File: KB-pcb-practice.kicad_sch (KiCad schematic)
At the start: 61 parts, among them J1 Conn_01x03, SW1 Reset, SW2 Boot, U1 RP2040, U2 IS31FL3742A-QFLS4-TR, U3 W25Q128JVS, U4 IS31FL3742A-QFLS4-TR, U5 NCP1117-3.3_SOT223, Y1 ABLS-12.000MHZ-B4-T

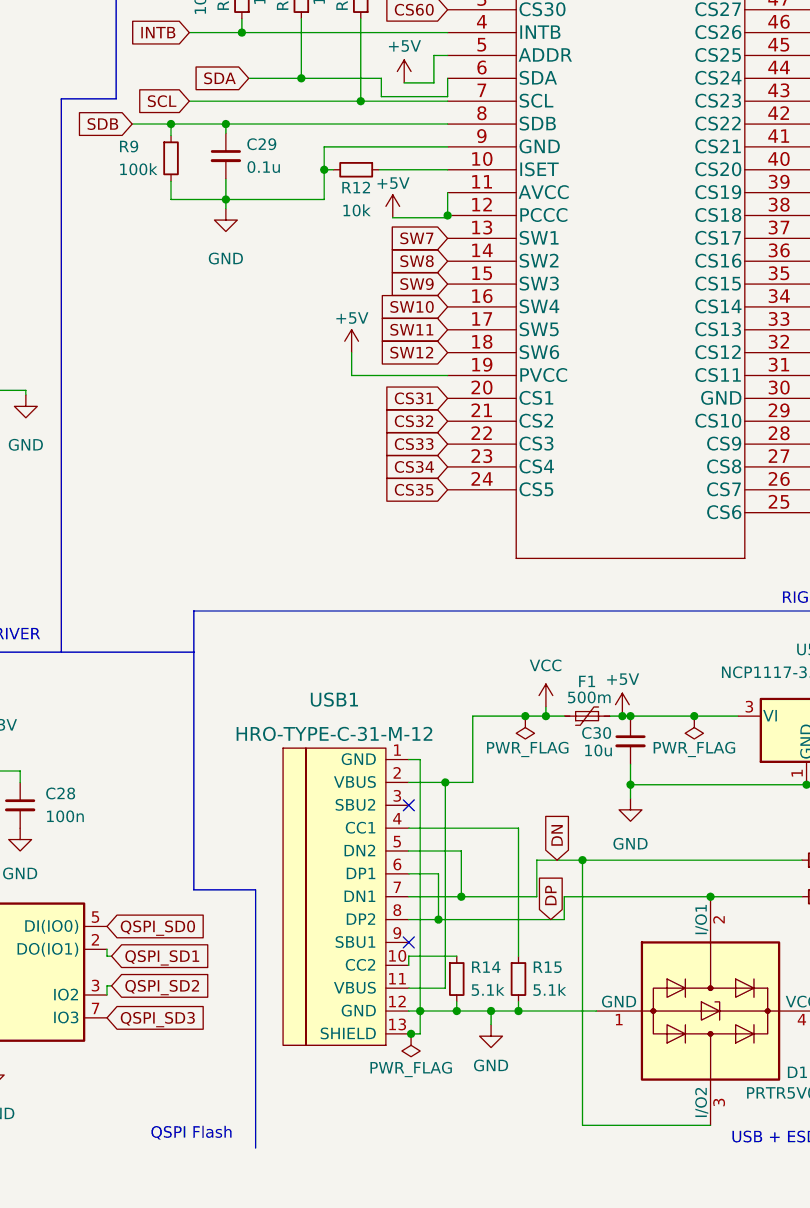
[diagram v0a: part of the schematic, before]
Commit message: Updated Schematic to match previous
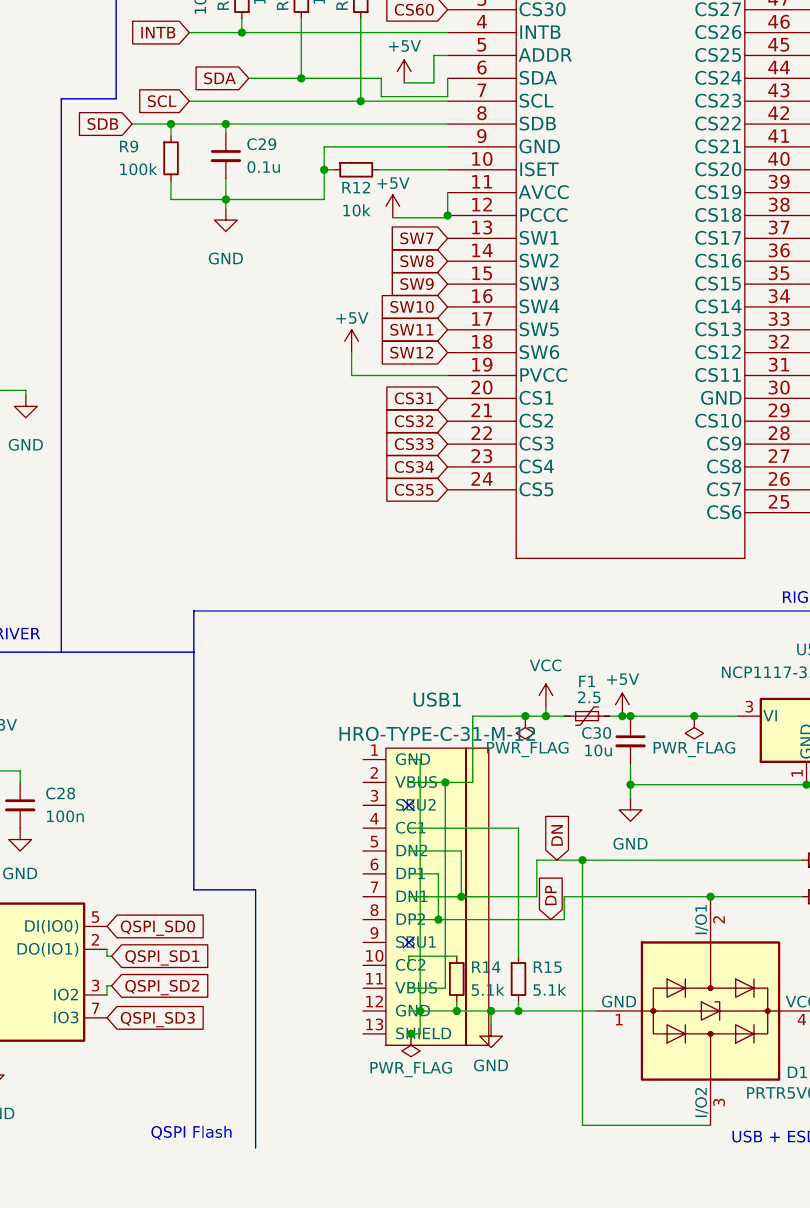
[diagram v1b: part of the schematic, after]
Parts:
- F1: value 500m -> 2.5
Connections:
- net DN: no longer USB1.5 (DN2), USB1.7 (DN1)
- net DP: no longer USB1.6 (DP1), USB1.8 (DP2)
- net GND: now also R12.1; no longer R12.2, USB1.1 (GND), USB1.12 (GND), USB1.13 (SHIELD)
- net VCC: no longer USB1.11 (VBUS), USB1.2 (VBUS)
- net at USB1.10 (CC2): no longer R14.1
- net at USB1.4 (CC1): no longer R15.1
- net at U4.10 (ISET): now also R12.2; no longer R12.1
- net  COL0 renamed COL0
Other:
- moved on the sheet: R12, USB1
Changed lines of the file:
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@@
     )
   )
-  (global_label " COL0" (shape input) (at 76.708 41.148 0) (fields_autoplaced)
+  (global_label "COL0" (shape input) (at 76.708 41.148 0) (fields_autoplaced)
     (effects (font (size 1.27 1.27)) (justify left))
-    (property "Intersheetrefs" "${INTERSHEET_REFS}" (at 85.4195 41.148 0)
+    (property "Intersheetrefs" "${INTERSHEET_REFS}" (at 84.4519 41.148 0)
       (effects (font (size 1.27 1.27)) (justify left) hide)
     )
@@
     )
   )
-  (symbol (lib_id "Type-C:HRO-TYPE-C-31-M-12") (at 222.504 136.906 0) (unit 1)
-    (in_bom yes) (on_board yes) (dnp no) (fields_autoplaced)
-    (property "Reference" "USB1" (at 216.789 116.332 0)
+  (symbol (lib_id "Type-C:HRO-TYPE-C-31-M-12") (at 222.504 136.906 0) (mirror y) (unit 1)
+    (in_bom yes) (on_board yes) (dnp no)
+    (property "Reference" "USB1" (at 228.219 116.332 0)
       (effects (font (size 1.524 1.524)))
     )
-    (property "Value" "HRO-TYPE-C-31-M-12" (at 216.789 120.142 0)
+    (property "Value" "HRO-TYPE-C-31-M-12" (at 228.219 120.142 0)
       (effects (font (size 1.524 1.524)))
     )
@@
     )
   )
-  (symbol (lib_id "Device:R_Small") (at 219.202 57.404 270) (unit 1)
+  (symbol (lib_id "Device:R_Small") (at 219.202 57.404 90) (mirror x) (unit 1)
     (in_bom yes) (on_board yes) (dnp no)
     (property "Reference" "R12" (at 219.202 59.436 90)
@@
       (effects (font (size 1.27 1.27)))
     )
-    (property "Value" "500m" (at 245.11 116.078 90)
-      (effects (font (size 1.27 1.27)))
-    )
+    (property "Value" "2.5" (at 245.11 116.078 90)
+      (effects (font (size 1.27 1.27)))
+    )

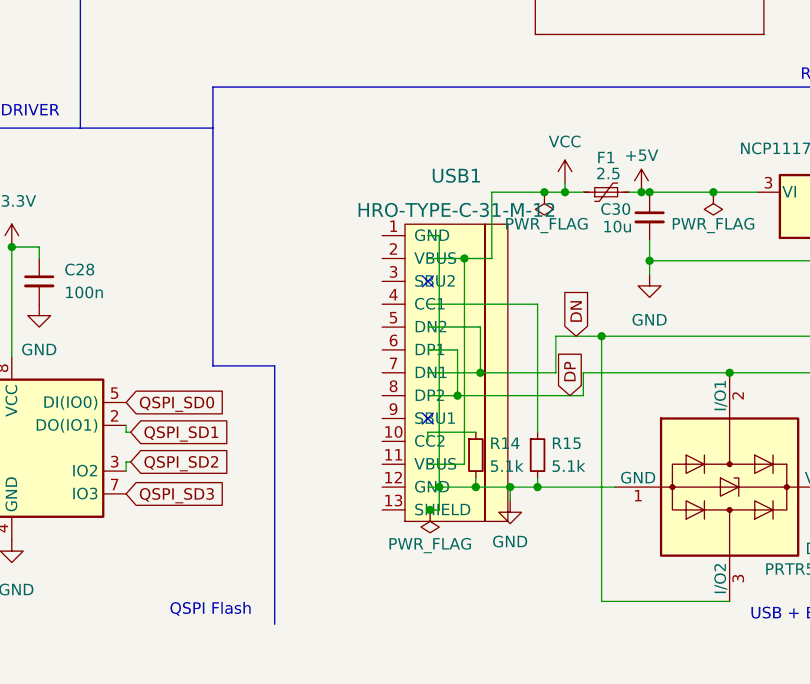
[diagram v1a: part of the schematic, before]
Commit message: Began Routing Columns and Rows
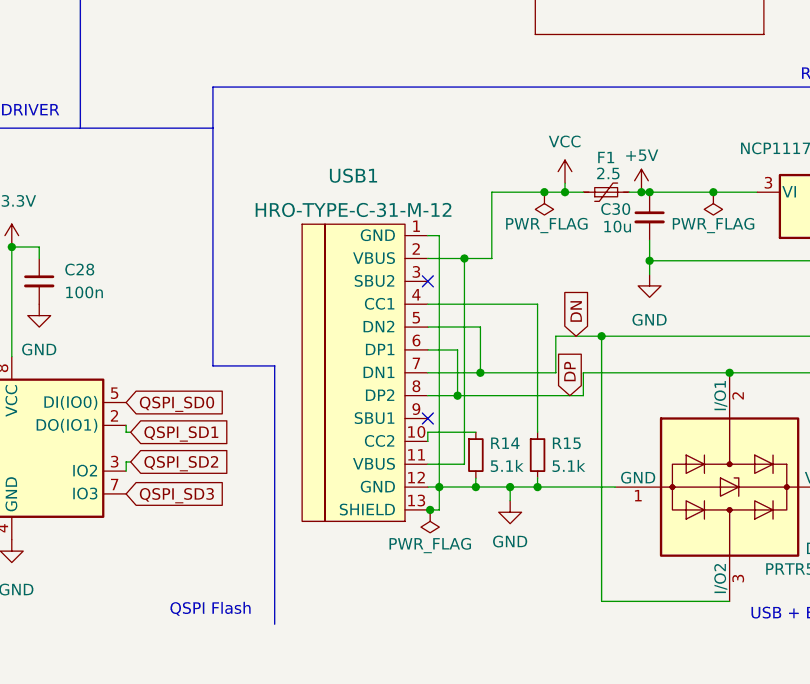
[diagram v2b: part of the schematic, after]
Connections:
- net DN: now also USB1.5 (DN2), USB1.7 (DN1)
- net DP: now also USB1.6 (DP1), USB1.8 (DP2)
- net GND: now also USB1.1 (GND), USB1.12 (GND), USB1.13 (SHIELD)
- net VCC: now also USB1.11 (VBUS), USB1.2 (VBUS)
- net at USB1.10 (CC2): now also R14.1
- net at USB1.4 (CC1): now also R15.1
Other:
- moved on the sheet: USB1
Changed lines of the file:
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@@
     )
   )
-  (symbol (lib_id "Type-C:HRO-TYPE-C-31-M-12") (at 222.504 136.906 0) (mirror y) (unit 1)
+  (symbol (lib_id "Type-C:HRO-TYPE-C-31-M-12") (at 222.504 136.906 0) (unit 1)
     (in_bom yes) (on_board yes) (dnp no)
-    (property "Reference" "USB1" (at 228.219 116.332 0)
+    (property "Reference" "USB1" (at 216.789 116.332 0)
       (effects (font (size 1.524 1.524)))
     )
-    (property "Value" "HRO-TYPE-C-31-M-12" (at 228.219 120.142 0)
+    (property "Value" "HRO-TYPE-C-31-M-12" (at 216.789 120.142 0)
       (effects (font (size 1.524 1.524)))
     )

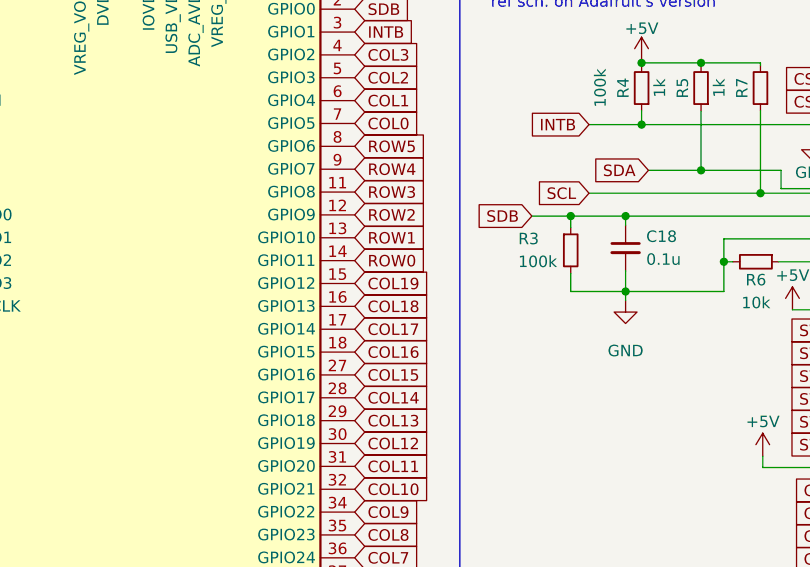
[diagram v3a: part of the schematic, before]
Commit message: Revising for underglow and PD IC
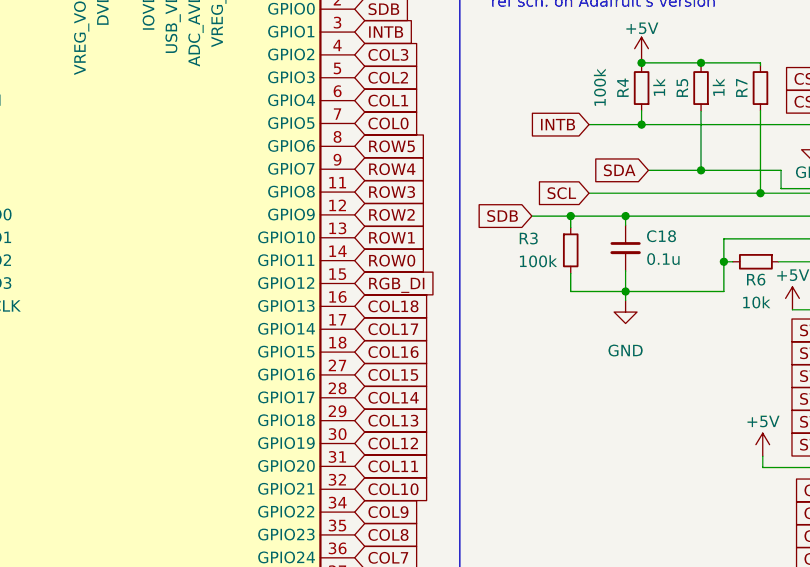
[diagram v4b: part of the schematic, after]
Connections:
- net COL19 renamed RGB_DI
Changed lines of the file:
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@@
     )
   )
-  (global_label "COL19" (shape input) (at 76.708 58.928 0) (fields_autoplaced)
+  (global_label "RGB_DI" (shape input) (at 76.708 58.928 0) (fields_autoplaced)
     (effects (font (size 1.27 1.27)) (justify left))
-    (property "Intersheetrefs" "${INTERSHEET_REFS}" (at 85.6614 58.928 0)
+    (property "Intersheetrefs" "${INTERSHEET_REFS}" (at 86.2662 58.928 0)
       (effects (font (size 1.27 1.27)) (justify left) hide)
     )

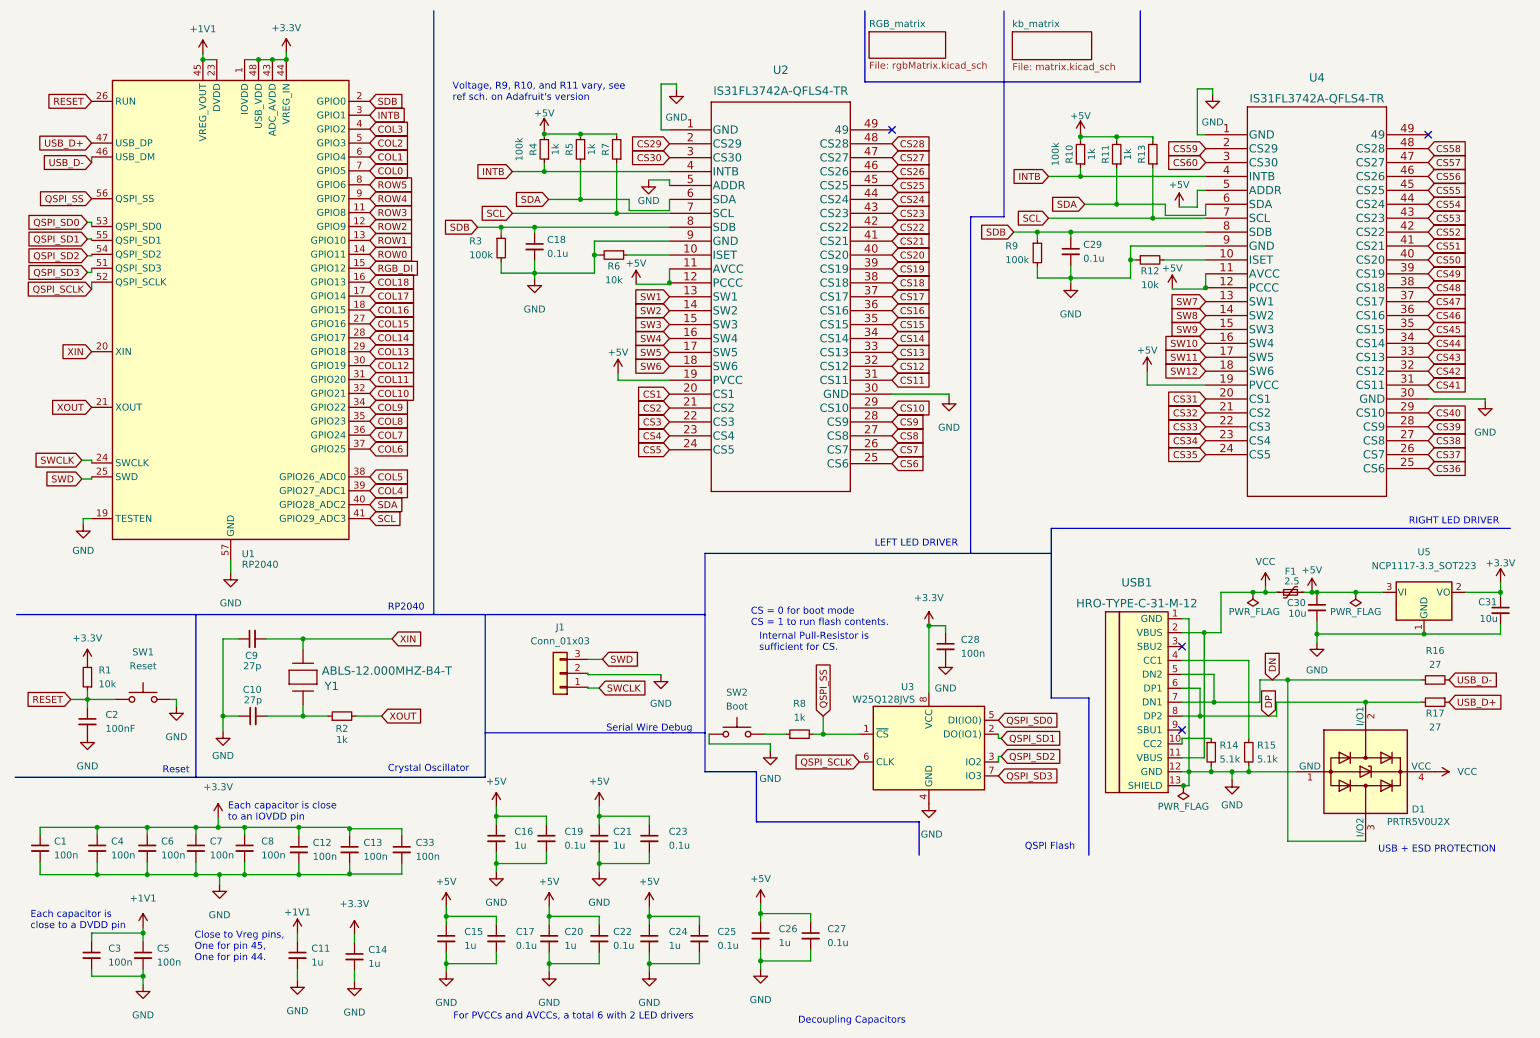
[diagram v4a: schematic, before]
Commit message: Rearranged LED Drivers
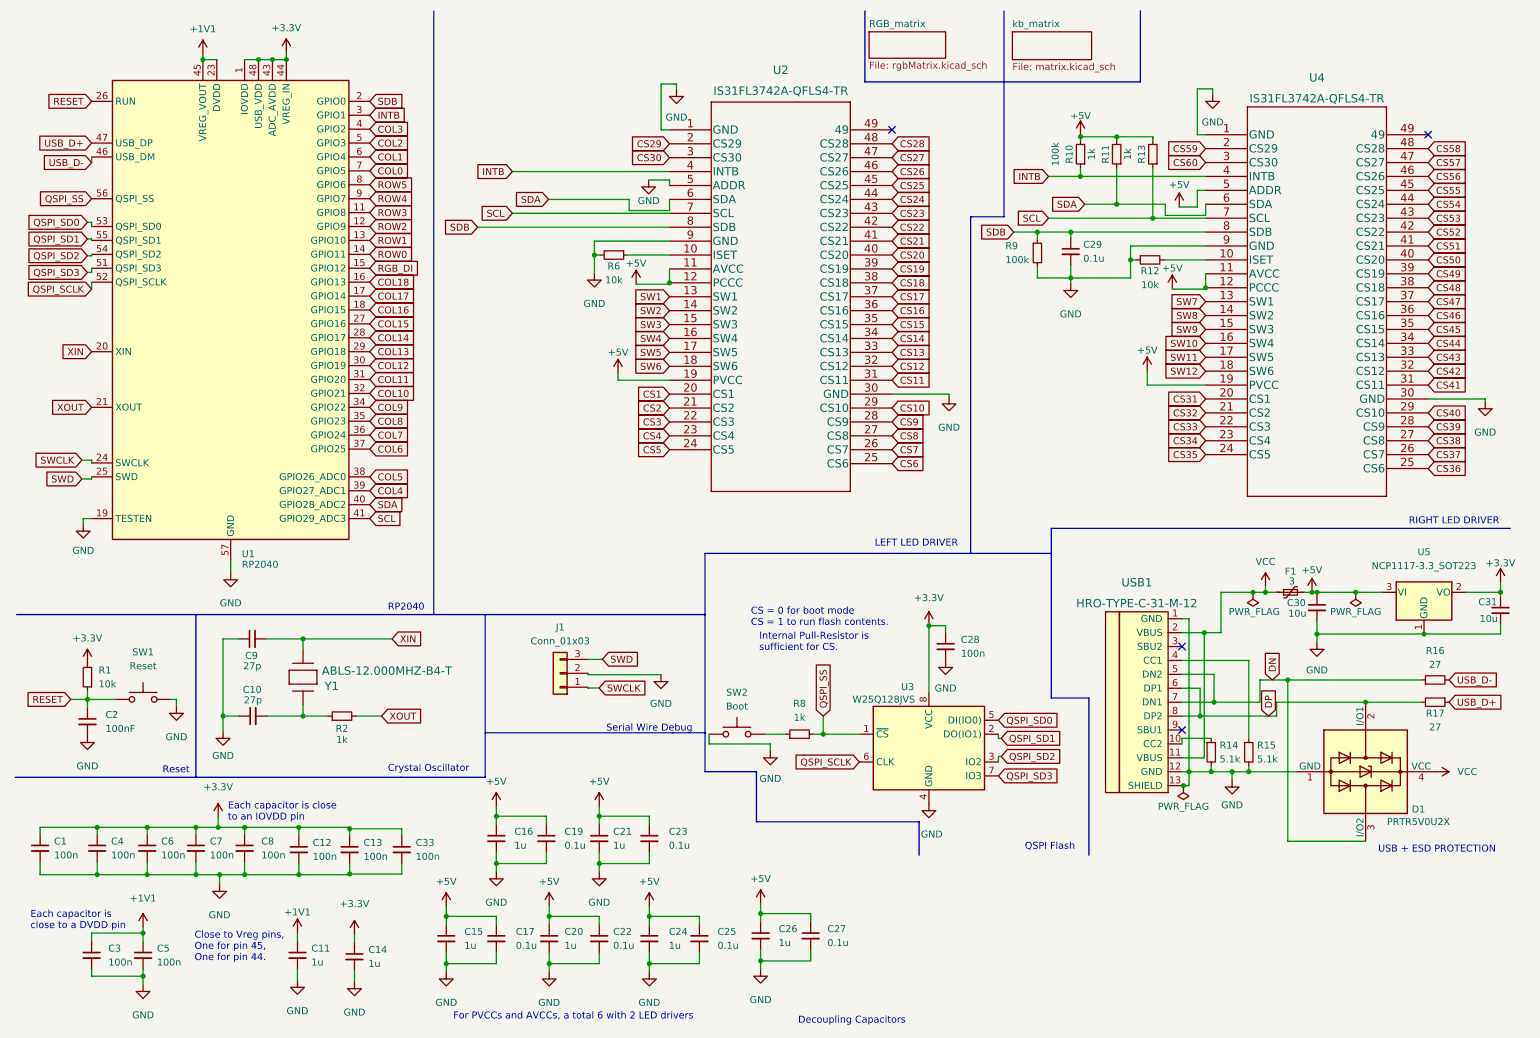
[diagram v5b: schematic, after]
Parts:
- removed C18: 0.1u, Capacitor_SMD:C_0805_2012Metric_Pad1.18x1.45mm_HandSolder, symbol Device:C_Small
- removed R3, R4: 100k, Resistor_SMD:R_0805_2012Metric_Pad1.20x1.40mm_HandSolder, symbol Device:R_Small
- removed R5, R7: 1k, Resistor_SMD:R_0805_2012Metric_Pad1.20x1.40mm_HandSolder, symbol Device:R_Small
- F1: value 2.5 -> 3
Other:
- note removed: "Voltage, R9, R10, and R11 vary, see ref sch. on Adafruit's version"
